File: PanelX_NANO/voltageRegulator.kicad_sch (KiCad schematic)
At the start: 4 parts

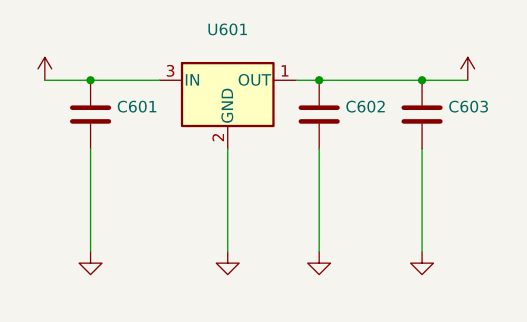
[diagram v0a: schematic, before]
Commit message: Deleted zip files from repo
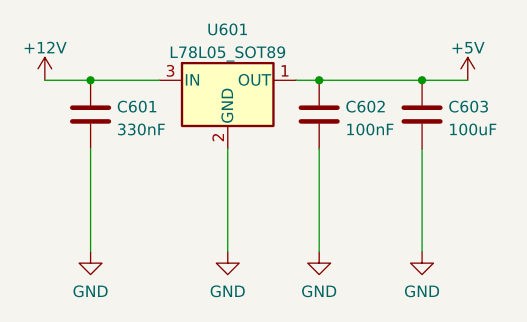
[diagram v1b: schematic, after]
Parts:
- C601: value (none) -> 330nF; footprint (none) -> Capacitor_SMD:C_0603_1608Metric_Pad1.08x0.95mm_HandSolder
- C602: value (none) -> 100nF; footprint (none) -> Capacitor_SMD:C_0603_1608Metric_Pad1.08x0.95mm_HandSolder
- C603: value (none) -> 100uF; footprint (none) -> Capacitor_SMD:C_1206_3216Metric_Pad1.33x1.80mm_HandSolder
- U601: value (none) -> L78L05_SOT89; footprint (none) -> Package_TO_SOT_SMD:SOT-89-3
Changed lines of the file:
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@@
       (effects (font (size 1.27 1.27)) hide)
     )
-    (property "Value" "" (id 1) (at 200.66 137.7934 0))
+    (property "Value" "GND" (id 1) (at 200.66 137.7934 0))
     (property "Footprint" "" (id 2) (at 200.66 133.35 0)
       (effects (font (size 1.27 1.27)) hide)
@@
       (effects (font (size 1.27 1.27)) (justify left))
     )
-    (property "Value" "" (id 1) (at 192.151 119.8122 0)
+    (property "Value" "100nF" (id 1) (at 192.151 119.8122 0)
       (effects (font (size 1.27 1.27)) (justify left))
     )
-    (property "Footprint" "" (id 2) (at 190.1952 121.92 0)
+    (property "Footprint" "Capacitor_SMD:C_0603_1608Metric_Pad1.08x0.95mm_HandSolder" (id 2) (at 190.1952 121.92 0)
       (effects (font (size 1.27 1.27)) hide)
     )
@@
     (in_bom yes) (on_board yes) (fields_autoplaced)
     (property "Reference" "U601" (id 0) (at 179.07 108.6952 0))
-    (property "Value" "" (id 1) (at 179.07 111.2321 0))
-    (property "Footprint" "" (id 2) (at 179.07 109.22 0)
+    (property "Value" "L78L05_SOT89" (id 1) (at 179.07 111.2321 0))
+    (property "Footprint" "Package_TO_SOT_SMD:SOT-89-3" (id 2) (at 179.07 109.22 0)
       (effects (font (size 1.27 1.27) italic) hide)
     )
@@
       (effects (font (size 1.27 1.27)) hide)
     )
-    (property "Value" "" (id 1) (at 205.74 110.7242 0))
+    (property "Value" "+5V" (id 1) (at 205.74 110.7242 0))
     (property "Footprint" "" (id 2) (at 205.74 114.3 0)
       (effects (font (size 1.27 1.27)) hide)
@@
       (effects (font (size 1.27 1.27)) hide)
     )
-    (property "Value" "" (id 1) (at 189.23 137.7934 0))
+    (property "Value" "GND" (id 1) (at 189.23 137.7934 0))
     (property "Footprint" "" (id 2) (at 189.23 133.35 0)
       (effects (font (size 1.27 1.27)) hide)
@@
       (effects (font (size 1.27 1.27)) hide)
     )
-    (property "Value" "" (id 1) (at 158.75 110.7242 0))
+    (property "Value" "+12V" (id 1) (at 158.75 110.7242 0))
     (property "Footprint" "" (id 2) (at 158.75 114.3 0)
       (effects (font (size 1.27 1.27)) hide)
@@
       (effects (font (size 1.27 1.27)) hide)
     )
-    (property "Value" "" (id 1) (at 163.83 137.7934 0))
+    (property "Value" "GND" (id 1) (at 163.83 137.7934 0))
     (property "Footprint" "" (id 2) (at 163.83 133.35 0)
       (effects (font (size 1.27 1.27)) hide)
@@
       (effects (font (size 1.27 1.27)) (justify left))
     )
-    (property "Value" "" (id 1) (at 166.751 119.8122 0)
+    (property "Value" "330nF" (id 1) (at 166.751 119.8122 0)
       (effects (font (size 1.27 1.27)) (justify left))
     )
-    (property "Footprint" "" (id 2) (at 164.7952 121.92 0)
+    (property "Footprint" "Capacitor_SMD:C_0603_1608Metric_Pad1.08x0.95mm_HandSolder" (id 2) (at 164.7952 121.92 0)
       (effects (font (size 1.27 1.27)) hide)
     )
@@
       (effects (font (size 1.27 1.27)) (justify left))
     )
-    (property "Value" "" (id 1) (at 203.581 119.8122 0)
+    (property "Value" "100uF" (id 1) (at 203.581 119.8122 0)
       (effects (font (size 1.27 1.27)) (justify left))
     )
-    (property "Footprint" "" (id 2) (at 201.6252 121.92 0)
+    (property "Footprint" "Capacitor_SMD:C_1206_3216Metric_Pad1.33x1.80mm_HandSolder" (id 2) (at 201.6252 121.92 0)
       (effects (font (size 1.27 1.27)) hide)
     )
@@
       (effects (font (size 1.27 1.27)) hide)
     )
-    (property "Value" "" (id 1) (at 179.07 137.7934 0))
+    (property "Value" "GND" (id 1) (at 179.07 137.7934 0))
     (property "Footprint" "" (id 2) (at 179.07 133.35 0)
       (effects (font (size 1.27 1.27)) hide)

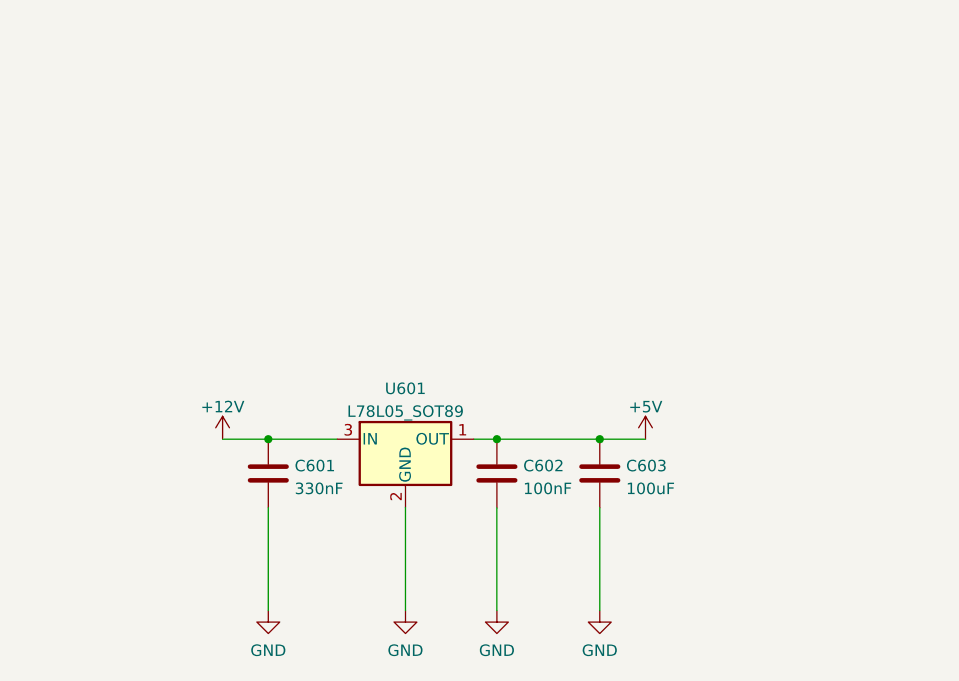
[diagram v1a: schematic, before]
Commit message: I picked a suitable connector. I will use plain 2x12 female n male connectors for the b2b connector. Death to flatcables! The RJ12 connector still goed on the panel carrier board. I will look for vertical SMD variant
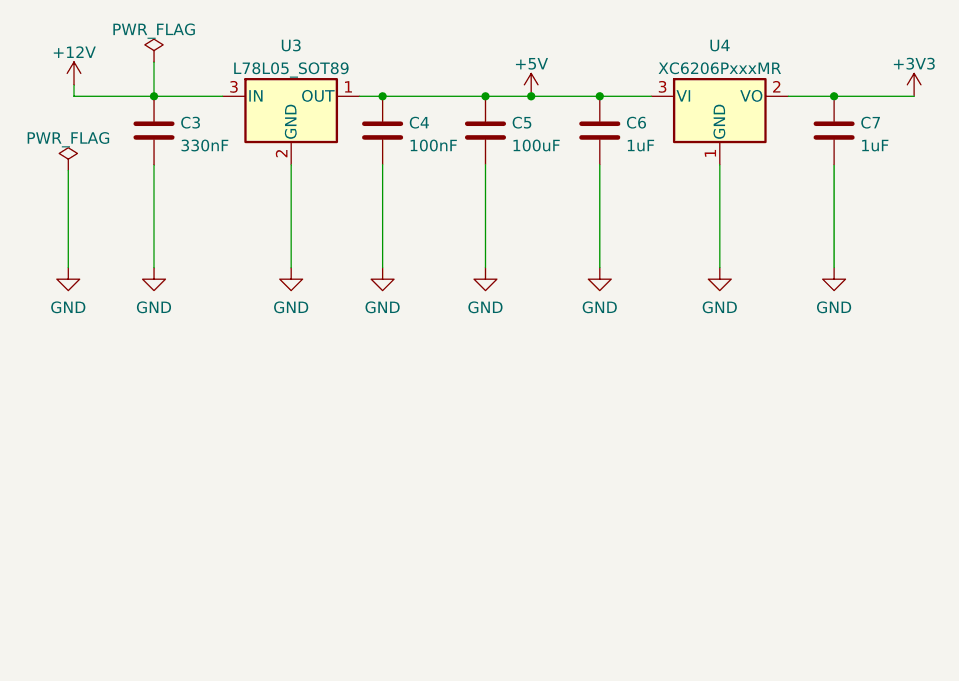
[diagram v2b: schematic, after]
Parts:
- removed C601: 330nF, Capacitor_SMD:C_0603_1608Metric_Pad1.08x0.95mm_HandSolder, symbol Device:C
- removed C602: 100nF, Capacitor_SMD:C_0603_1608Metric_Pad1.08x0.95mm_HandSolder, symbol Device:C
- removed C603: 100uF, Capacitor_SMD:C_1206_3216Metric_Pad1.33x1.80mm_HandSolder, symbol Device:C
- removed U601: L78L05_SOT89, Package_TO_SOT_SMD:SOT-89-3, symbol Regulator_Linear:L78L05_SOT89
- added C3: 330nF, Capacitor_SMD:C_0603_1608Metric_Pad1.08x0.95mm_HandSolder, symbol Device:C
- added C4: 100nF, Capacitor_SMD:C_0603_1608Metric_Pad1.08x0.95mm_HandSolder, symbol Device:C
- added C5: 100uF, Capacitor_SMD:C_1206_3216Metric_Pad1.33x1.80mm_HandSolder, symbol Device:C
- added C6, C7: 1uF, Capacitor_SMD:C_0603_1608Metric_Pad1.08x0.95mm_HandSolder, symbol Device:C
- added U3: L78L05_SOT89, Package_TO_SOT_SMD:SOT-89-3, symbol Regulator_Linear:L78L05_SOT89
- added U4: XC6206PxxxMR, Package_TO_SOT_SMD:SOT-23, symbol Regulator_Linear:XC6206PxxxMR
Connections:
- net +12V: now also C3.1, U3.3 (IN)
- net +5V: now also C4.1, C5.1, C6.1, U3.1 (OUT), U4.3 (VI)
- net GND: now also C3.2, C4.2, C5.2, C6.2, C7.2, U3.2 (GND), U4.1 (GND)
- new net +3V3: C7.1, U4.2 (VO)
